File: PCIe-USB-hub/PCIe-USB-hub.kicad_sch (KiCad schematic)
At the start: 2 parts, among them J1 Bus_PCI_Express_x1, J2 USB3_A_Stacked

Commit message: Создал основные компоненты, поставил на схеме
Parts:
- removed J1: Bus_PCI_Express_x1, Connector_PCBEdge:BUS_PCIexpress_x1, symbol Connector:Bus_PCI_Express_x1
- removed J2: USB3_A_Stacked, Connector_USB:USB3_A_Molex_48406-0001_Horizontal_Stacked, symbol Connector:USB3_A_Stacked
- added J1: PCIexpress_x1, PCIexpress:PCIexpress_x1, symbol PCIexpress:PCIexpress_x1
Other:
- added sheet PCIe to USB (PCIe to USB.kicad_sch)
- added sheet USB (USB.kicad_sch)
- added sheet USB host to USB hub (USB host to USB hub.kicad_sch)

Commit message: Частично добавил компоненты
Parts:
- added J7: ATX-20, symbol Connector:ATX-20
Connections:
- new net: J7.1 (+3.3V), J7.11 (+3.3V), J7.2 (+3.3V)
- new net: J7.13 (GND), J7.15 (GND), J7.16 (GND), J7.17 (GND), J7.3 (GND), J7.5 (GND), J7.7 (GND)
- new net: J7.19 (+5V), J7.20 (+5V), J7.4 (+5V), J7.6 (+5V)
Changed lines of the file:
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@@
 	(paper "A3")
+	(symbol
+		(lib_id "Connector:ATX-20")
+		(at 257.81 77.47 0)
+		(unit 1)
+		(exclude_from_sim no)
+		(in_bom yes)
+		(on_board yes)
+		(dnp no)
+		(fields_autoplaced yes)
+		(property "Reference" "J7"
+			(at 257.81 59.69 0)
+			(effects
+				(font
+					(size 1.27 1.27)
+				)
+			)
+		)
+		(property "Value" "ATX-20"
+			(at 257.81 62.23 0)
+			(effects
+				(font
+					(size 1.27 1.27)
+				)
+			)
+		)
+		(property "Footprint" ""
+			(at 257.81 80.01 0)
+			(effects
+				(font
+					(size 1.27 1.27)
+				)
+				(hide yes)
+			)
+		)
+		(property "Datasheet" "https://web.aub.edu.lb/pub/docs/atx_201.pdf#page=20"
+			(at 285.75 91.44 0)
+			(effects
+				(font
+					(size 1.27 1.27)
+				)
+				(hide yes)
+			)
+		)
+		(property "Description" "ATX Power supply 20pins"
+			(at 257.81 77.47 0)
+			(effects
+				(font
+					(size 1.27 1.27)
+				)
+				(hide yes)
+			)
+		)
+		(pin "11"
+		)
+		(pin "8"
+		)
+		(pin "9"
+		)
+		(pin "15"
+		)
+		(pin "16"
+		)
+		(pin "5"
+		)
+		(pin "10"
+		)
+		(pin "19"
+		)
+		(pin "3"
+		)
+		(pin "6"
+		)
+		(pin "1"
+		)
+		(pin "14"
+		)
+		(pin "13"
+		)
+		(pin "17"
+		)
+		(pin "7"
+		)
+		(pin "4"
+		)
+		(pin "20"
+		)
+		(pin "18"
+		)
+		(pin "2"
+		)
+		(pin "12"
+		)
+		(instances
+			(project ""
+				(path "/9ca96bdf-018d-455b-a724-78a2bbb0adec"
+					(reference "J7")
+					(unit 1)
+				)
+			)
+		)
+	)
 	(symbol
 		(lib_id "PCIexpress:PCIexpress_x1")
@@
 		(on_board yes)
 		(dnp no)
-		(fields_autoplaced yes)
 		(property "Reference" "J1"
 			(at 173.99 76.2 0)
@@
 		)
 		(property "Value" "PCIexpress_x1"
-			(at 173.99 78.74 0)
+			(at 173.482 133.604 0)
 			(effects
 				(font

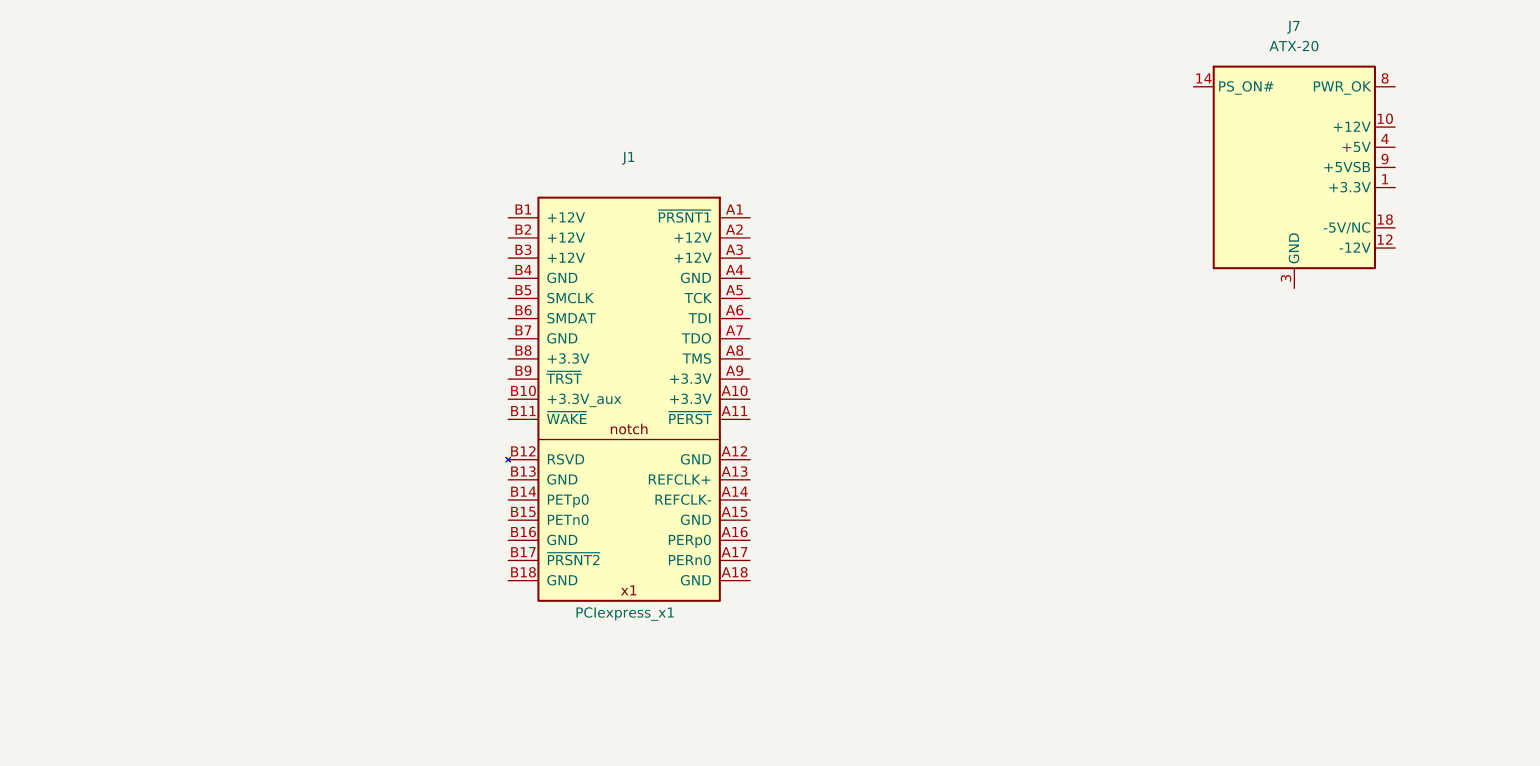
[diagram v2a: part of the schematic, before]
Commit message: Изменение иерархии схемы + на схеме теперь все линии USB соединены
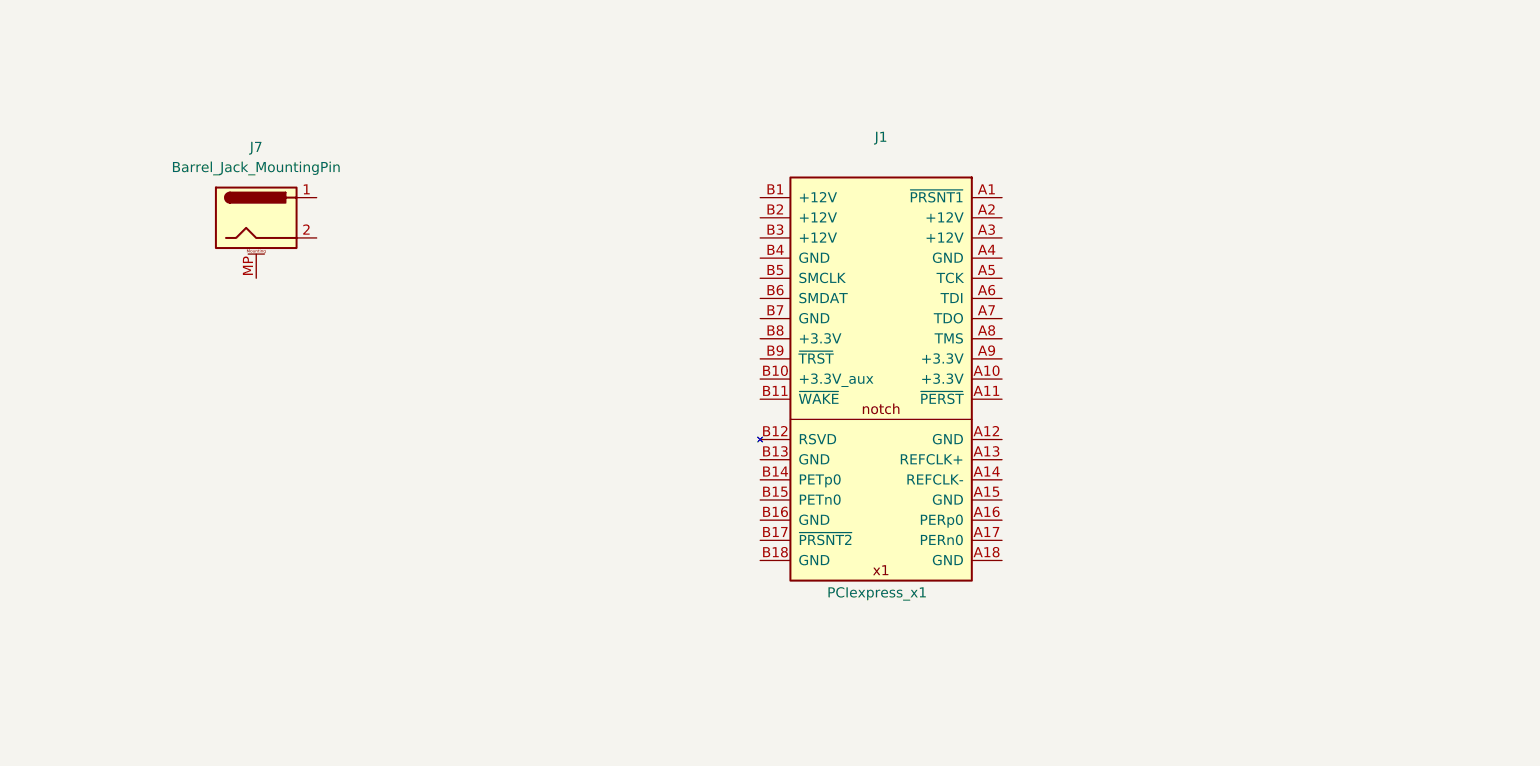
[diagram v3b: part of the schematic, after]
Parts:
- removed J7: ATX-20, symbol Connector:ATX-20
- added J7: Barrel_Jack_MountingPin, Connector_BarrelJack:BarrelJack_GCT_DCJ200-10-A_Horizontal, symbol Connector:Barrel_Jack_MountingPin
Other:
- moved on the sheet: J1
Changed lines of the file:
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@@
 	(paper "A3")
 	(symbol
-		(lib_id "Connector:ATX-20")
-		(at 257.81 77.47 0)
+		(lib_id "Connector:Barrel_Jack_MountingPin")
+		(at 127 83.82 0)
 		(unit 1)
 		(exclude_from_sim no)
@@
 		(fields_autoplaced yes)
 		(property "Reference" "J7"
-			(at 257.81 59.69 0)
+			(at 127 74.93 0)
 			(effects
 				(font
@@
 			)
 		)
-		(property "Value" "ATX-20"
-			(at 257.81 62.23 0)
+		(property "Value" "Barrel_Jack_MountingPin"
+			(at 127 77.47 0)
 			(effects
 				(font
@@
 			)
 		)
-		(property "Footprint" ""
-			(at 257.81 80.01 0)
+		(property "Footprint" "Connector_BarrelJack:BarrelJack_GCT_DCJ200-10-A_Horizontal"
+			(at 128.27 84.836 0)
 			(effects
 				(font
@@
 			)
 		)
-		(property "Datasheet" "https://web.aub.edu.lb/pub/docs/atx_201.pdf#page=20"
-			(at 285.75 91.44 0)
+		(property "Datasheet" "~"
+			(at 128.27 84.836 0)
 			(effects
 				(font
@@
 			)
 		)
-		(property "Description" "ATX Power supply 20pins"
-			(at 257.81 77.47 0)
+		(property "Description" "DC Barrel Jack with a mounting pin"
+			(at 127 83.82 0)
 			(effects
 				(font
@@
 			)
 		)
-		(pin "11"
-		)
-		(pin "8"
-		)
-		(pin "9"
-		)
-		(pin "15"
-		)
-		(pin "16"
-		)
-		(pin "5"
-		)
-		(pin "10"
-		)
-		(pin "19"
-		)
-		(pin "3"
-		)
-		(pin "6"
+		(pin "2"
 		)
 		(pin "1"
 		)
-		(pin "14"
-		)
-		(pin "13"
-		)
-		(pin "17"
-		)
-		(pin "7"
-		)
-		(pin "4"
-		)
-		(pin "20"
-		)
-		(pin "18"
-		)
-		(pin "2"
-		)
-		(pin "12"
+		(pin "MP"
 		)
 		(instances
@@
 	(symbol
 		(lib_id "PCIexpress:PCIexpress_x1")
-		(at 173.99 81.28 0)
+		(at 205.74 78.74 0)
 		(unit 1)
 		(exclude_from_sim no)
@@
 		(dnp no)
 		(property "Reference" "J1"
-			(at 173.99 76.2 0)
+			(at 205.74 73.66 0)
 			(effects
 				(font
@@
 		)
 		(property "Value" "PCIexpress_x1"
-			(at 173.482 133.604 0)
+			(at 205.232 131.064 0)
 			(effects
 				(font
@@
 		)
 		(property "Footprint" "PCIexpress:PCIexpress_x1"
-			(at 173.99 105.41 0)
+			(at 205.74 102.87 0)
 			(effects
 				(font
@@
 		)
 		(property "Datasheet" ""
-			(at 173.99 105.41 0)
+			(at 205.74 102.87 0)
 			(effects
 				(font
@@
 		)
 		(property "Description" ""
-			(at 173.99 81.28 0)
+			(at 205.74 78.74 0)
 			(effects
 				(font

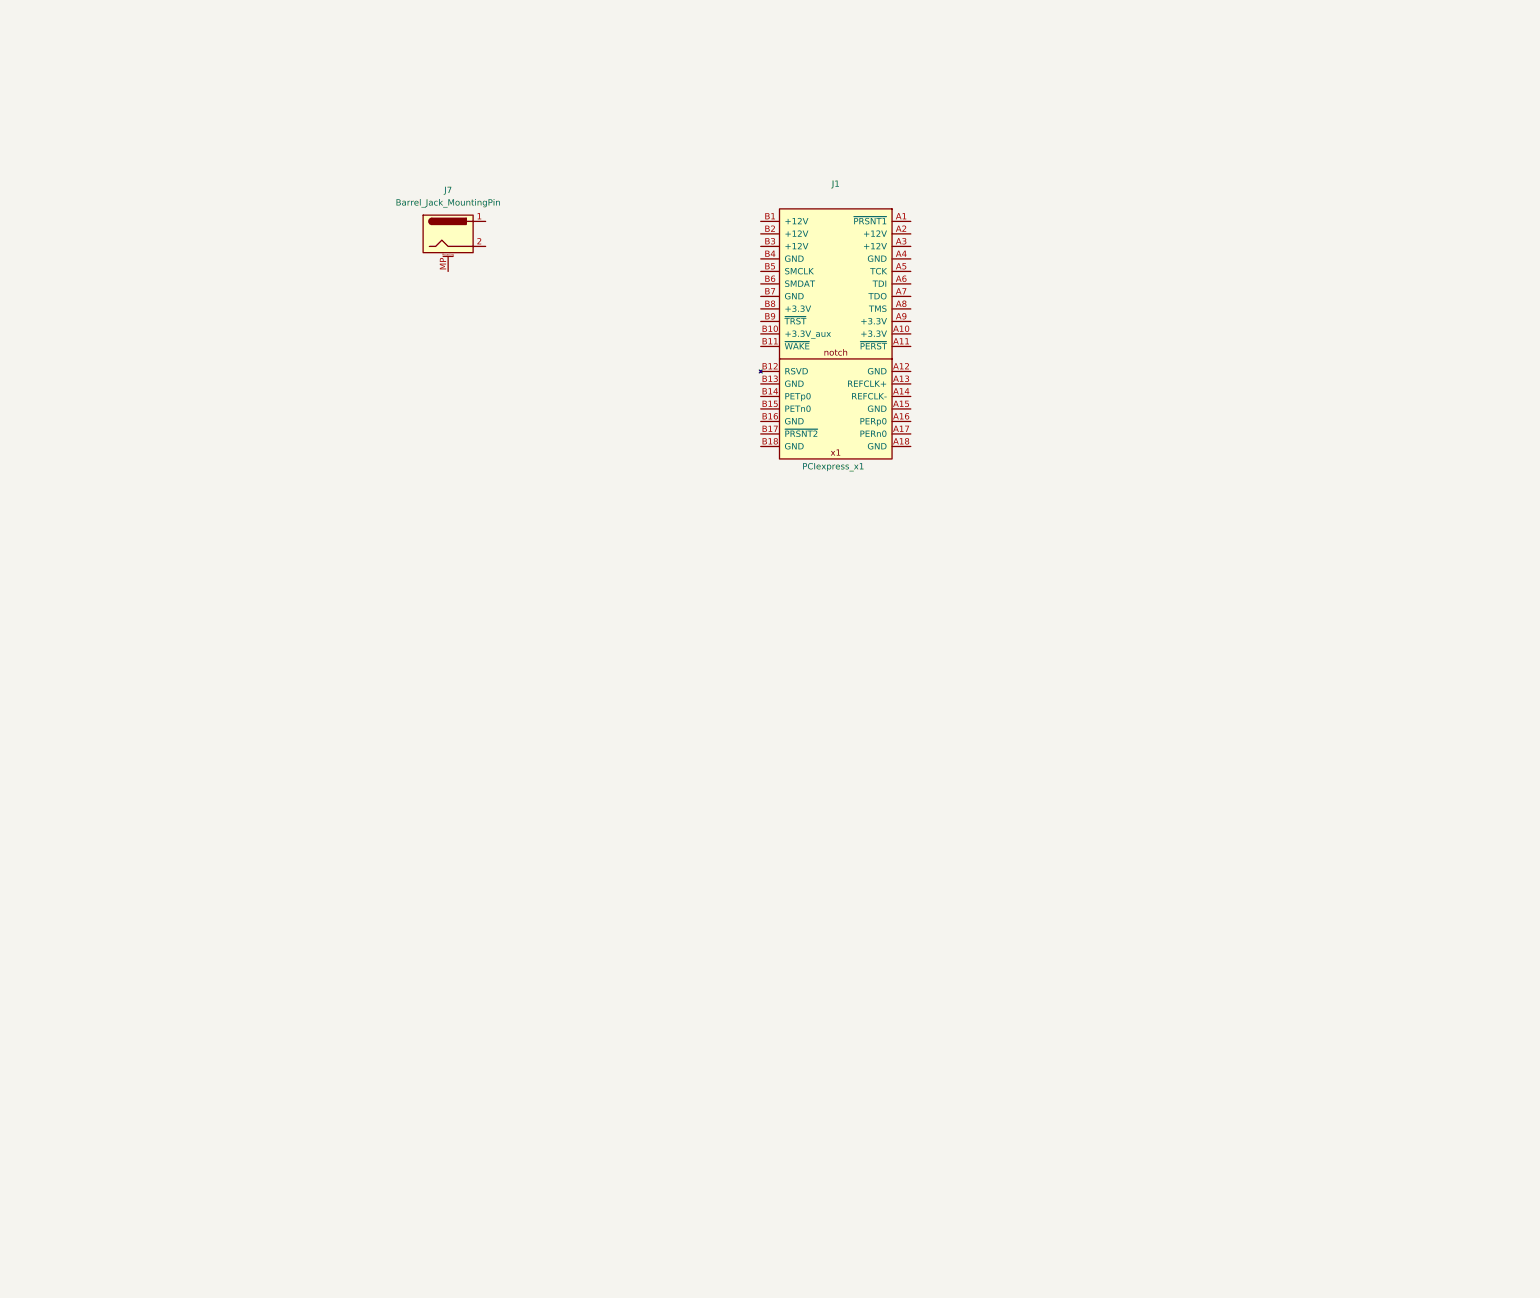
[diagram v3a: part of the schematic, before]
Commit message: Исправил отсутствие перекрёстного соединения на  PCIe
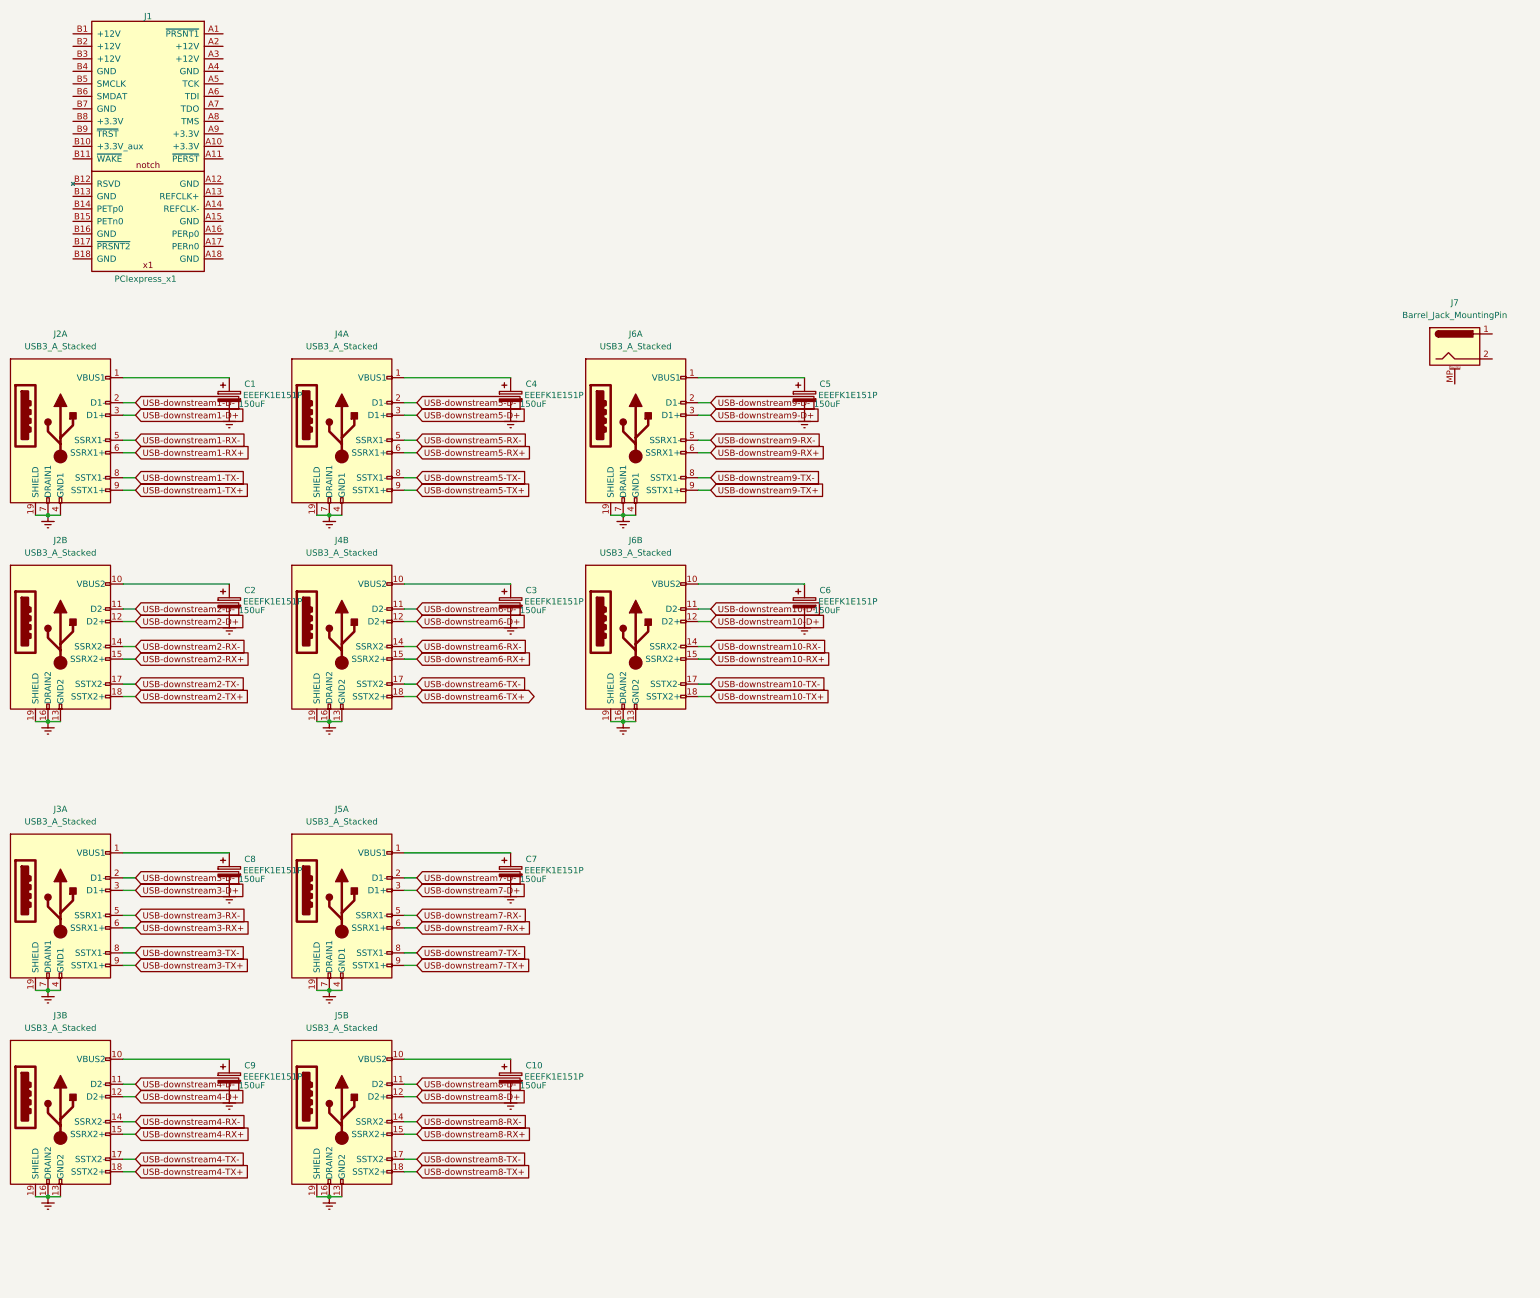
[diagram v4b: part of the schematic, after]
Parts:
- added C1, C10, C2, C3, C4, C5, C6, C7, C8, C9: EEEFK1E151P, Capacitor_SMD:C_Elec_8x10.2, symbol Device:C_Polarized
- added J2, J3, J4, J5, J6: USB3_A_Stacked, Connector_USB:USB3_A_Molex_48406-0001_Horizontal_Stacked, symbol Connector:USB3_A_Stacked
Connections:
- new net: C8.1, J3.1 (VBUS1)
- new net: C3.1, J4.10 (VBUS2)
- new net: C7.1, J5.1 (VBUS1)
- new net: C9.1, J3.10 (VBUS2)
- new net: C6.1, J6.10 (VBUS2)
- new net: C5.1, J6.1 (VBUS1)
- new net: C1.1, J2.1 (VBUS1)
- new net: C10.1, J5.10 (VBUS2)
- new net: C2.1, J2.10 (VBUS2)
- new net: C4.1, J4.1 (VBUS1)
- new net Earth: C1.2, C10.2, C2.2, C3.2, C4.2, C5.2, C6.2, C7.2, C8.2, C9.2, J2.13 (GND2), J2.16 (DRAIN2), J2.19 (SHIELD), J2.19 (SHIELD), J2.4 (GND1), J2.7 (DRAIN1), J3.13 (GND2), J3.16 (DRAIN2), J3.19 (SHIELD), J3.19 (SHIELD), J3.4 (GND1), J3.7 (DRAIN1), J4.13 (GND2), J4.16 (DRAIN2), J4.19 (SHIELD), J4.19 (SHIELD), J4.4 (GND1), J4.7 (DRAIN1), J5.13 (GND2), J5.16 (DRAIN2), J5.19 (SHIELD), J5.19 (SHIELD), J5.4 (GND1), J5.7 (DRAIN1), J6.13 (GND2), J6.16 (DRAIN2), J6.19 (SHIELD), J6.19 (SHIELD), J6.4 (GND1), J6.7 (DRAIN1)
- new net USB-downstream1-D+: J2.3 (D1+)
- new net USB-downstream1-D-: J2.2 (D1-)
- new net USB-downstream1-RX+: J2.6 (SSRX1+)
- new net USB-downstream1-RX-: J2.5 (SSRX1-)
- new net USB-downstream1-TX+: J2.9 (SSTX1+)
- new net USB-downstream1-TX-: J2.8 (SSTX1-)
- new net USB-downstream10-D+: J6.12 (D2+)
- new net USB-downstream10-D-: J6.11 (D2-)
- new net USB-downstream10-RX+: J6.15 (SSRX2+)
- new net USB-downstream10-RX-: J6.14 (SSRX2-)
- new net USB-downstream10-TX+: J6.18 (SSTX2+)
- new net USB-downstream10-TX-: J6.17 (SSTX2-)
- new net USB-downstream2-D+: J2.12 (D2+)
- new net USB-downstream2-D-: J2.11 (D2-)
- new net USB-downstream2-RX+: J2.15 (SSRX2+)
- new net USB-downstream2-RX-: J2.14 (SSRX2-)
- new net USB-downstream2-TX+: J2.18 (SSTX2+)
- new net USB-downstream2-TX-: J2.17 (SSTX2-)
- new net USB-downstream3-D+: J3.3 (D1+)
- new net USB-downstream3-D-: J3.2 (D1-)
- new net USB-downstream3-RX+: J3.6 (SSRX1+)
- new net USB-downstream3-RX-: J3.5 (SSRX1-)
- new net USB-downstream3-TX+: J3.9 (SSTX1+)
- new net USB-downstream3-TX-: J3.8 (SSTX1-)
- new net USB-downstream4-D+: J3.12 (D2+)
- new net USB-downstream4-D-: J3.11 (D2-)
- new net USB-downstream4-RX+: J3.15 (SSRX2+)
- new net USB-downstream4-RX-: J3.14 (SSRX2-)
- new net USB-downstream4-TX+: J3.18 (SSTX2+)
- new net USB-downstream4-TX-: J3.17 (SSTX2-)
- new net USB-downstream5-D+: J4.3 (D1+)
- new net USB-downstream5-D-: J4.2 (D1-)
- new net USB-downstream5-RX+: J4.6 (SSRX1+)
- new net USB-downstream5-RX-: J4.5 (SSRX1-)
- new net USB-downstream5-TX+: J4.9 (SSTX1+)
- new net USB-downstream5-TX-: J4.8 (SSTX1-)
- new net USB-downstream6-D+: J4.12 (D2+)
- new net USB-downstream6-D-: J4.11 (D2-)
- new net USB-downstream6-RX+: J4.15 (SSRX2+)
- new net USB-downstream6-RX-: J4.14 (SSRX2-)
- new net USB-downstream6-TX+: J4.18 (SSTX2+)
- new net USB-downstream6-TX-: J4.17 (SSTX2-)
- new net USB-downstream7-D+: J5.3 (D1+)
- new net USB-downstream7-D-: J5.2 (D1-)
- new net USB-downstream7-RX+: J5.6 (SSRX1+)
- new net USB-downstream7-RX-: J5.5 (SSRX1-)
- new net USB-downstream7-TX+: J5.9 (SSTX1+)
- new net USB-downstream7-TX-: J5.8 (SSTX1-)
- new net USB-downstream8-D+: J5.12 (D2+)
- new net USB-downstream8-D-: J5.11 (D2-)
- new net USB-downstream8-RX+: J5.15 (SSRX2+)
- new net USB-downstream8-RX-: J5.14 (SSRX2-)
- new net USB-downstream8-TX+: J5.18 (SSTX2+)
- new net USB-downstream8-TX-: J5.17 (SSTX2-)
- new net USB-downstream9-D+: J6.3 (D1+)
- new net USB-downstream9-D-: J6.2 (D1-)
- new net USB-downstream9-RX+: J6.6 (SSRX1+)
- new net USB-downstream9-RX-: J6.5 (SSRX1-)
- new net USB-downstream9-TX+: J6.9 (SSTX1+)
- new net USB-downstream9-TX-: J6.8 (SSTX1-)
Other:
- moved on the sheet: J1, J7

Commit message: Чут изменений
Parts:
- added C39, C40, C41, C42: 100nF, Capacitor_SMD:C_0402_1005Metric, symbol Device:C
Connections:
- net at J1.A1 (~{PRSNT1}): now also J1.B17 (~{PRSNT2})
- net PCIe-CLK+: now reaches J1.A13 (REFCLK+)
- net PCIe-CLK-: now reaches J1.A14 (REFCLK-)
- net at J1.A16 (PERp0): now also C40.2
- net at J1.A17 (PERn0): now also C39.2
- net at J1.A6 (TDI): now also J1.A7 (TDO)
- net at J1.B14 (PETp0): now also C42.2
- net at J1.B15 (PETn0): now also C41.2
- new net PCIe-RX+: C42.1
- new net PCIe-RX-: C41.1
- new net PCIe-TX+: C40.1
- new net PCIe-TX-: C39.1
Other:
- moved on the sheet: J1

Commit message: Доработка схемы, частичная конфигурация чипов
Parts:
- added DD3: TPS2552DRVR, Package_SON:WSON-6-1EP_2x2mm_P0.65mm_EP1x1.6mm, symbol TPS2552DRVR:TPS2552DRVR
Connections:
- net +5V_USB3: now reaches C8.1, J3.1 (VBUS1)
- net +5V_USB6: now reaches C3.1, J4.10 (VBUS2)
- net +5V_USB7: now reaches C7.1, J5.1 (VBUS1)
- net +5V_USB4: now reaches C9.1, J3.10 (VBUS2)
- net +5V_USB10: now reaches C6.1, J6.10 (VBUS2)
- net +5V_USB9: now reaches C5.1, J6.1 (VBUS1)
- net +5V_USB1: now reaches C1.1, J2.1 (VBUS1)
- net +5V_USB8: now reaches C10.1, J5.10 (VBUS2)
- net +5V_USB2: now reaches C2.1, J2.10 (VBUS2)
- net +5V_USB5: now reaches C4.1, J4.1 (VBUS1)
- net PERST_PCIe: now reaches J1.A11 (~{PERST})
- net WAKE_PCIe: now reaches J1.B11 (~{WAKE})
- no-connect marks 0 -> 5
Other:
- removed sheet USB
